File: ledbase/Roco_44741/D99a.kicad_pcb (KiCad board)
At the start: 2 copper layers, 297.7 x 22.4 mm, 90 parts, among them J1 Conn_01x01, J10 Conn_01x01, J11 Conn_01x01, J12 Conn_01x04, J13 Conn_01x06, J2 Conn_01x01, J3 Conn_01x01, J4 Conn_01x01, J5 Conn_02x10_Odd_Even, J6 Conn_01x01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

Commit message: add: ledbase Roco_44741
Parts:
- C3, C4, C6: value 330u/16V -> 470u/16V
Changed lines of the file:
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@@
 			)
 		)
-		(property "Value" "330u/16V"
+		(property "Value" "470u/16V"
 			(at 0 3.95 90)
 			(layer "F.Fab")
@@
 			)
 		)
-		(property "Description" ""
+		(property "Description" "-55℃~+105℃ 16V 470uF 70mΩ@100kHz ±20% CASE-H-7360-20(mm) Tantalum Capacitors ROHS"
 			(at 0 0 90)
 			(layer "F.Fab")
@@
 			)
 		)
+		(property "LCSC Part #" "C600599"
+			(at 0 0 270)
+			(unlocked yes)
+			(layer "F.Fab")
+			(hide yes)
+			(effects
+				(font
+					(size 1 1)
+					(thickness 0.15)
+				)
+			)
+		)
 		(property ki_fp_filters "CP_*")
 		(sheetname "/Base/")
@@
 			)
 		)
-		(property "Value" "330u/16V"
+		(property "Value" "470u/16V"
 			(at 0 3.95 90)
 			(layer "F.Fab")
@@
 			)
 		)
+		(property "LCSC Part #" "C600599"
+			(at 0 0 270)
+			(unlocked yes)
+			(layer "F.Fab")
+			(hide yes)
+			(effects
+				(font
+					(size 1 1)
+					(thickness 0.15)
+				)
+			)
+		)
 		(property ki_fp_filters "CP_*")
 		(sheetname "/Base/")
@@
 			)
 		)
-		(property "Value" "330u/16V"
+		(property "Value" "470u/16V"
 			(at 0 3.95 90)
 			(layer "F.Fab")
@@
 			)
 		)
+		(property "LCSC Part #" "C600599"
+			(at 0 0 270)
+			(unlocked yes)
+			(layer "F.Fab")
+			(hide yes)
+			(effects
+				(font
+					(size 1 1)
+					(thickness 0.15)
+				)
+			)
+		)
 		(property ki_fp_filters "CP_*")
 		(sheetname "/Base/")
@@
 			)
 		)
-		(property "Description" "-55℃~+155℃ 100mW 1kΩ 75V Thick Film Resistor ±1% ±100ppm/℃ 0603 Chip Resistor - Surface Mount ROHS"
+		(property "Description" "-55℃~+155℃ 120Ω 50V 62.5mW Thick Film Resistor ±1% ±100ppm/℃ 0402 Chip Resistor - Surface Mount ROHS"
 			(at 0 0 180)
 			(layer "F.Fab")
@@
 			)
 		)
-		(property "JLCPCB" "C21190"
+		(property "JLCPCB" "C25079"
 			(at 0 0 180)
 			(unlocked yes)
@@
 			)
 		)
-		(property "Description" ""
+		(property "Description" "-55℃~+155℃ 330kΩ 50V 62.5mW Thick Film Resistor ±1% ±100ppm/℃ 0402 Chip Resistor - Surface Mount ROHS"
 			(at 0 0 180)
 			(layer "F.Fab")
@@
 			)
 		)
+		(property "LCSC Part #" "C25778"
+			(at 0 0 180)
+			(unlocked yes)
+			(layer "F.Fab")
+			(hide yes)
+			(effects
+				(font
+					(size 1 1)
+					(thickness 0.15)
+				)
+			)
+		)
 		(property ki_fp_filters "R_*")
 		(sheetname "/SPI/LED/")
@@
 			)
 		)
-		(property "Description" ""
+		(property "Description" "-55℃~+155℃ 22kΩ 50V 62.5mW Thick Film Resistor ±1% ±100ppm/℃ 0402 Chip Resistor - Surface Mount ROHS"
 			(at 0 0 0)
 			(layer "F.Fab")
@@
 			)
 		)
+		(property "LCSC Part #" "C25768"
+			(at 0 0 0)
+			(unlocked yes)
+			(layer "F.Fab")
+			(hide yes)
+			(effects
+				(font
+					(size 1 1)
+					(thickness 0.15)
+				)
+			)
+		)
 		(property ki_fp_filters "R_*")
 		(sheetname "/SPI/LED/")
@@
 			)
 		)
-		(property "Description" ""
+		(property "Description" "-55℃~+155℃ 330kΩ 50V 62.5mW Thick Film Resistor ±1% ±100ppm/℃ 0402 Chip Resistor - Surface Mount ROHS"
 			(at 0 0 0)
 			(layer "F.Fab")
@@
 			)
 		)
+		(property "LCSC Part #" "C25778"
+			(at 0 0 0)
+			(unlocked yes)
+			(layer "F.Fab")
+			(hide yes)
+			(effects
+				(font
+					(size 1 1)
+					(thickness 0.15)
+				)
+			)
+		)
 		(property ki_fp_filters "R_*")
 		(sheetname "/SPI/LED/")
@@
 			)
 		)
+		(property "LCSC Part #" ""
+			(at 0 0 0)
+			(unlocked yes)
+			(layer "F.Fab")
+			(hide yes)
+			(effects
+				(font
+					(size 1 1)
+					(thickness 0.15)
+				)
+			)
+		)
 		(property ki_fp_filters "*SC?70*")
 		(sheetname "/SPI/LED/")
@@
 			)
 		)
+		(property "LCSC Part #" ""
+			(at 0 0 180)
+			(unlocked yes)
+			(layer "F.Fab")
+			(hide yes)
+			(effects
+				(font
+					(size 1 1)
+					(thickness 0.15)
+				)
+			)
+		)
 		(property ki_fp_filters "C_*")
 		(sheetname "/SPI/LED/")
@@
 			)
 		)
-		(property "Description" ""
+		(property "Description" "-40℃~+125℃ 19ns@4.5V,50pF 2V~6V 74HC 8 Serial-to-Serial or Parallel Tri-State DHVQFN-16-EP(2.5x3.5) Shift Registers ROHS"
 			(at 0 0 0)
 			(layer "B.Fab")
@@
 			)
 		)
+		(property "LCSC Part #" "C730243"
+			(at 0 0 180)
+			(unlocked yes)
+			(layer "B.Fab")
+			(hide yes)
+			(effects
+				(font
+					(size 1 1)
+					(thickness 0.15)
+				)
+				(justify mirror)
+			)
+		)
 		(property ki_fp_filters "DIP*W7.62mm* SOIC*3.9x9.9mm*P1.27mm* TSSOP*4.4x5mm*P0.65mm* SOIC*5.3x10.2mm*P1.27mm* SOIC*7.5x10.3mm*P1.27mm*")
 		(sheetname "/SPI/LED/")
@@
 			)
 		)
-		(property "Description" ""
+		(property "Description" "-40℃~+125℃ 19ns@4.5V,50pF 2V~6V 74HC 8 Serial-to-Serial or Parallel Tri-State DHVQFN-16-EP(2.5x3.5) Shift Registers ROHS"
 			(at 0 0 0)
 			(layer "B.Fab")
@@
 			)
 		)
+		(property "LCSC Part #" "C730243"
+			(at 0 0 180)
+			(unlocked yes)
+			(layer "B.Fab")
+			(hide yes)
+			(effects
+				(font
+					(size 1 1)
+					(thickness 0.15)
+				)
+				(justify mirror)
+			)
+		)
 		(property ki_fp_filters "DIP*W7.62mm* SOIC*3.9x9.9mm*P1.27mm* TSSOP*4.4x5mm*P0.65mm* SOIC*5.3x10.2mm*P1.27mm* SOIC*7.5x10.3mm*P1.27mm*")
 		(sheetname "/SPI/LED/")
@@
 			)
 		)
-		(property "Description" ""
+		(property "Description" "-40℃~+125℃ 19ns@4.5V,50pF 2V~6V 74HC 8 Serial-to-Serial or Parallel Tri-State DHVQFN-16-EP(2.5x3.5) Shift Registers ROHS"
 			(at 0 0 0)
 			(layer "B.Fab")
@@
 			)
 		)
+		(property "LCSC Part #" "C730243"
+			(at 0 0 180)
+			(unlocked yes)
+			(layer "B.Fab")
+			(hide yes)
+			(effects
+				(font
+					(size 1 1)
+					(thickness 0.15)
+				)
+				(justify mirror)
+			)
+		)
 		(property ki_fp_filters "DIP*W7.62mm* SOIC*3.9x9.9mm*P1.27mm* TSSOP*4.4x5mm*P0.65mm* SOIC*5.3x10.2mm*P1.27mm* SOIC*7.5x10.3mm*P1.27mm*")
 		(sheetname "/SPI/LED/")
@@
 			)
 		)
-		(property "Description" ""
+		(property "Description" "-40℃~+125℃ 19ns@4.5V,50pF 2V~6V 74HC 8 Serial-to-Serial or Parallel Tri-State DHVQFN-16-EP(2.5x3.5) Shift Registers ROHS"
 			(at 0 0 0)
 			(layer "B.Fab")
@@
 			)
 		)
+		(property "LCSC Part #" "C730243"
+			(at 0 0 180)
+			(unlocked yes)
+			(layer "B.Fab")
+			(hide yes)
+			(effects
+				(font
+					(size 1 1)
+					(thickness 0.15)
+				)
+				(justify mirror)
+			)
+		)
 		(property ki_fp_filters "DIP*W7.62mm* SOIC*3.9x9.9mm*P1.27mm* TSSOP*4.4x5mm*P0.65mm* SOIC*5.3x10.2mm*P1.27mm* SOIC*7.5x10.3mm*P1.27mm*")
 		(sheetname "/SPI/LED/")
@@
 			)
 		)
-		(property "Description" ""
+		(property "Description" "-40℃~+100℃ 150mW 16V 400nm~690nm 5nA 60° 620nm SMD Photodiodes ROHS"
 			(at 0 0 90)
 			(unlocked yes)
@@
 					(thickness 0.15)
 				)
+				(justify mirror)
+			)
+		)
+		(property "LCSC Part #" "C2900227"
+			(at 0 0 270)
+			(unlocked yes)
+			(layer "B.Fab")
+			(hide yes)
+			(effects
+				(font
+					(size 1 1)
+					(thickness 0.15)
+				)

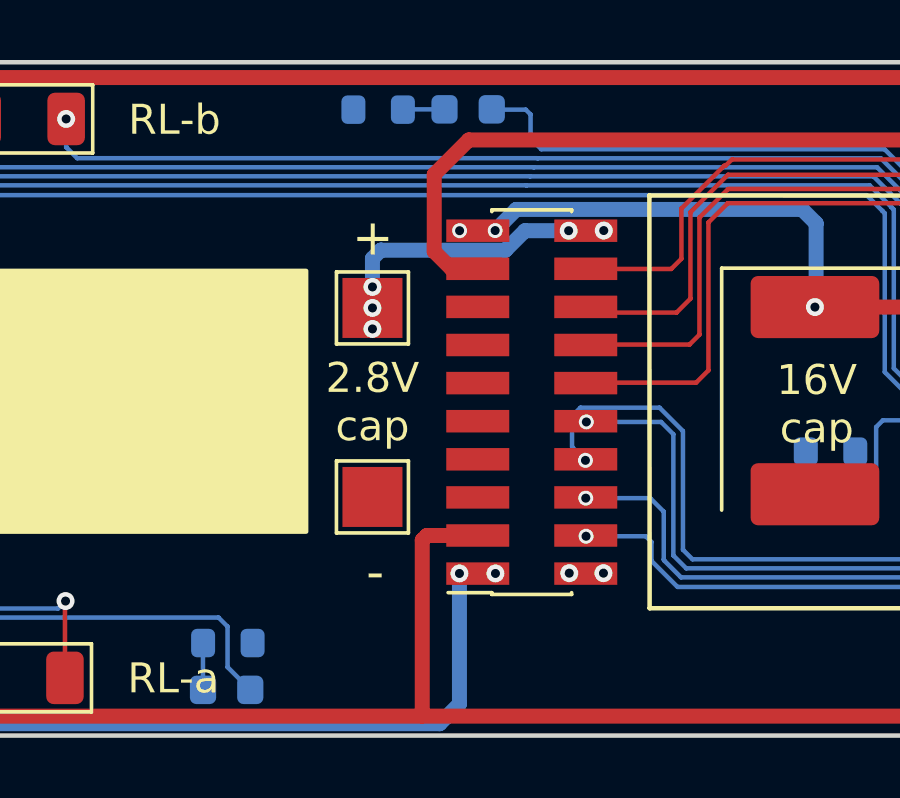
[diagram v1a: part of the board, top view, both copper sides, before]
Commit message: mod: ncap leakage resistor
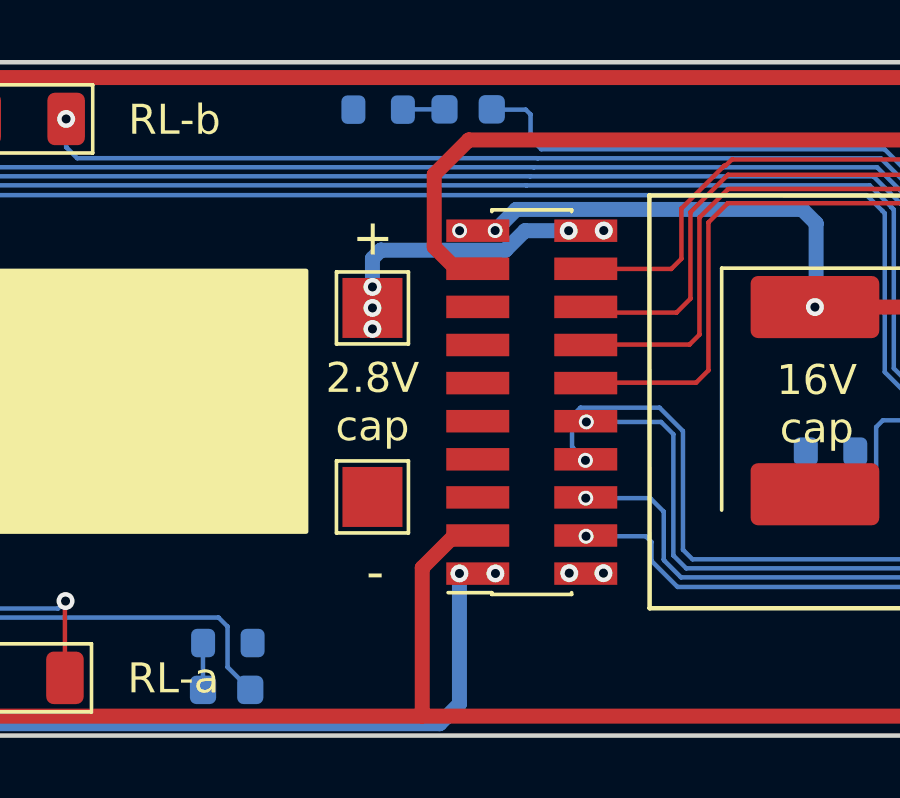
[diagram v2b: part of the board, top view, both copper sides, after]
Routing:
- net DCC-a: track 317.6 -> 317.0 mm
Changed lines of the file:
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@@
-	)
-	(segment
-		(start 80.15 -70.885)
-		(end 78.455 -70.885)
-		(width 0.5)
-		(layer "F.Cu")
-		(net 6)
 	)
 	(segment
@@
 	)
 	(segment
-		(start 78.455 -70.885)
-		(end 78.3 -70.73)
-		(width 0.5)
-		(layer "F.Cu")
-		(net 6)
-	)
-	(segment
-		(start 78.3 -70.73)
-		(end 78.3 -64.864)
-		(width 0.5)
-		(layer "F.Cu")
-		(net 6)
-	)
-	(segment
 		(start 54.08 -70.94)
 		(end 54.08 -73.94)
@@
 	)
 	(segment
+		(start 79.375 -70.885)
+		(end 78.3 -69.81)
+		(width 0.5)
+		(layer "F.Cu")
+		(net 6)
+	)
+	(segment
 		(start 80.15 -70.885)
 		(end 80.125 -70.91)
@@
 	)
 	(segment
+		(start 78.3 -69.81)
+		(end 78.3 -64.864)
+		(width 0.5)
+		(layer "F.Cu")
+		(net 6)
+	)
+	(segment
 		(start 344.72 -71.12)
 		(end 347.36 -71.12)
+		(width 0.5)
+		(layer "F.Cu")
+		(net 6)
+	)
+	(segment
+		(start 80.15 -70.885)
+		(end 79.375 -70.885)
 		(width 0.5)
 		(layer "F.Cu")
@@
 	)
 	(segment
-		(start 78.699999 -80.349999)
-		(end 78.699999 -82.919999)
+		(start 79.850001 -84.070001)
+		(end 118.749999 -84.070001)
+		(width 0.5)
+		(layer "F.Cu")
+		(net 60)
+	)
+	(segment
+		(start 79.425 -79.775)
+		(end 78.699999 -80.500001)
 		(width 0.5)
 		(layer "F.Cu")
@@
 	)
 	(segment
-		(start 79.274998 -79.775)
-		(end 78.699999 -80.349999)
+		(start 125.665 -81.435)
+		(end 118.76 -81.435)
+		(width 0.5)
+		(layer "F.Cu")
+		(net 60)
+	)
+	(segment
+		(start 80.15 -79.775)
+		(end 79.425 -79.775)
+		(width 0.5)
+		(layer "F.Cu")
+		(net 60)
+	)
+	(segment
+		(start 126.07 -81.03)
+		(end 126.03 -81.07)
+		(width 0.5)
+		(layer "F.Cu")
+		(net 60)
+	)
+	(segment
+		(start 126.07 -76.79)
+		(end 126.07 -81.03)
 		(width 0.5)
 		(layer "F.Cu")
@@
 	)
 	(segment
-		(start 79.850001 -84.070001)
-		(end 118.749999 -84.070001)
-		(width 0.5)
-		(layer "F.Cu")
-		(net 60)
-	)
-	(segment
-		(start 80.15 -79.775)
-		(end 79.274998 -79.775)
-		(width 0.5)
-		(layer "F.Cu")
-		(net 60)
-	)
-	(segment
-		(start 125.665 -81.435)
-		(end 118.76 -81.435)
-		(width 0.5)
-		(layer "F.Cu")
-		(net 60)
-	)
-	(segment
-		(start 126.07 -81.03)
-		(end 126.03 -81.07)
-		(width 0.5)
-		(layer "F.Cu")
-		(net 60)
-	)
-	(segment
-		(start 126.07 -76.79)
-		(end 126.07 -81.03)
-		(width 0.5)
-		(layer "F.Cu")
+		(start 78.699999 -80.500001)
+		(end 78.699999 -82.919999)
+		(width 0.5)
+		(layer "F.Cu")
